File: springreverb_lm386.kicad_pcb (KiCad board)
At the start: 2 copper layers, 69.9 x 55.3 mm, 53 parts, among them J1 IN, J10 VR2_3, J11 VR_2_2, J12 To, J13 FromSW, J16 FromGND, J17 From, J18 VR_4_1, J19 VR4_3, J2 INGND, J20 VR3_1, J3 GND, J4 Vin, J5 LEDGND, J6 VR1_3, J7 VR_1_1, J8 toC6, J9 toC7, U1 TL072, U2 TC1044S, U3 LM386

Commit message: 入力のコンデンサの値を変更
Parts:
- C6: value 0.022u -> 4700p
- C7: value 0.01u -> 470p
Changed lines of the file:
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@@
 			)
 		)
-		(property "Value" "0.01u"
+		(property "Value" "470p"
 			(at 0.05 0.9 90)
 			(unlocked yes)
@@
 			)
 		)
-		(property "Value" "0.022u"
+		(property "Value" "4700p"
 			(at 0.05 0.9 90)
 			(unlocked yes)
@@
 	)
 	(zone
-		(net "Net-(J15-In)")
+		(net "Net-(C3-Pad1)")
 		(layer "B.Cu")
 		(hatch none 0.1)
-		(priority 30015)
+		(priority 30000)
 		(attr
 			(teardrop
@@
 		(polygon
 			(pts
-				(xy 95.5404 89.1376) (xy 93.7404 89.1376) (xy 93.6404 90.1376) (xy 94.6404 91.2886) (xy 95.6404 90.1376)
+				(xy 66.7148 105.373009) (xy 68.5148 105.373009) (xy 68.6148 103.591071) (xy 67.6148 103.272009)
+				(xy 66.6148 103.828978)
 			)
 		)
 	)
 	(zone
-		(net "Net-(U1C-V-)")
+		(net "Net-(C3-Pad1)")
 		(layer "B.Cu")
 		(hatch none 0.1)
-		(priority 30017)
+		(priority 30006)
 		(attr
 			(teardrop
@@
 		(polygon
 			(pts
-				(xy 97.547 78.44473) (xy 95.747 78.44473) (xy 95.747 78.503213) (xy 96.010604 77.866817) (xy 94.947096 79.689252)
-				(xy 95.202722 79.947491) (xy 96.840547 79.723879) (xy 97.283396 79.139609) (xy 97.547 78.503213)
+				(xy 68.5148 103.549091) (xy 66.7148 103.549091) (xy 66.6148 105.192822) (xy 67.6148 105.650091)
+				(xy 68.6148 105.192822)
 			)
 		)
@@
 	)
 	(zone
-		(net "Net-(J1-Pin_1)")
+		(net "Net-(C3-Pad1)")
 		(layer "B.Cu")
 		(hatch none 0.1)
-		(priority 30014)
+		(priority 30010)
 		(attr
 			(teardrop
@@
 		(polygon
 			(pts
-				(xy 117.232 93.609) (xy 115.432 93.609) (xy 115.332 94.609) (xy 116.332 95.76) (xy 117.332 94.609)
+				(xy 66.71787 101.157478) (xy 65.445078 102.43027) (xy 66.53666 103.663273) (xy 67.567105 103.279505)
+				(xy 67.950873 102.24906)
 			)
 		)
 	)
 	(zone
-		(net "Net-(C3-Pad1)")
+		(net "Net-(J6-Pin_1)")
 		(layer "B.Cu")
 		(hatch none 0.1)
-		(priority 30005)
+		(priority 30016)
 		(attr
 			(teardrop
@@
 		(polygon
 			(pts
-				(xy 68.464 101.179791) (xy 66.664 101.179791) (xy 66.564 102.823522) (xy 67.564 103.280791) (xy 68.564 102.823522)
+				(xy 100.446 70.984) (xy 102.246 70.984) (xy 102.346 69.984) (xy 101.346 68.833) (xy 100.346 69.984)
 			)
 		)
 	)
 	(zone
-		(net "Net-(U1C-V+)")
+		(net "Net-(U1C-V-)")
 		(layer "B.Cu")
 		(hatch none 0.1)
-		(priority 30012)
+		(priority 30017)
 		(attr
 			(teardrop
@@
 		(polygon
 			(pts
-				(xy 105.540747 89.145) (xy 105.540747 87.345) (xy 104.396223 87.245) (xy 103.439747 88.245) (xy 103.439747 88.980609)
+				(xy 97.547 78.44473) (xy 95.747 78.44473) (xy 95.747 78.503213) (xy 96.010604 77.866817) (xy 94.947096 79.689252)
+				(xy 95.202722 79.947491) (xy 96.840547 79.723879) (xy 97.283396 79.139609) (xy 97.547 78.503213)
 			)
 		)
 	)
 	(zone
-		(net "Net-(U1C-V-)")
+		(net "GND")
 		(layer "B.Cu")
 		(hatch none 0.1)
-		(priority 30003)
+		(priority 30002)
 		(attr
 			(teardrop
@@
 		(polygon
 			(pts
-				(xy 86.2948 85.888991) (xy 84.4948 85.888991) (xy 84.3948 87.532722) (xy 85.3948 87.989991) (xy 86.3948 87.532722)
+				(xy 92.050391 76.189) (xy 92.050391 77.989) (xy 93.694122 78.089) (xy 94.151391 77.089) (xy 93.694122 76.089)
 			)
 		)
 	)
 	(zone
-		(net "Net-(C12-Pad2)")
+		(net "GND")
 		(layer "B.Cu")
 		(hatch none 0.1)
-		(priority 30008)
+		(priority 30013)
 		(attr
 			(teardrop
@@
 		(polygon
 			(pts
-				(xy 86.24093 97.724522) (xy 87.513722 96.45173) (xy 86.422139 95.218726) (xy 85.391695 95.602495)
-				(xy 85.007926 96.632939)
+				(xy 90.0062 90.7436) (xy 91.8062 90.7436) (xy 91.9062 89.7436) (xy 90.9062 88.4926) (xy 89.9062 89.7436)
 			)
 		)
@@
 		(layer "B.Cu")
 		(hatch none 0.1)
-		(priority 30010)
+		(priority 30005)
 		(attr
 			(teardrop
@@
 		(polygon
 			(pts
-				(xy 66.71787 101.157478) (xy 65.445078 102.43027) (xy 66.53666 103.663273) (xy 67.567105 103.279505)
-				(xy 67.950873 102.24906)
+				(xy 68.464 101.179791) (xy 66.664 101.179791) (xy 66.564 102.823522) (xy 67.564 103.280791) (xy 68.564 102.823522)
 			)
 		)
@@
 	)
 	(zone
-		(net "GND")
+		(net "Net-(J15-In)")
 		(layer "B.Cu")
 		(hatch none 0.1)
-		(priority 30013)
+		(priority 30015)
 		(attr
 			(teardrop
@@
 		(polygon
 			(pts
-				(xy 90.0062 90.7436) (xy 91.8062 90.7436) (xy 91.9062 89.7436) (xy 90.9062 88.4926) (xy 89.9062 89.7436)
+				(xy 95.5404 89.1376) (xy 93.7404 89.1376) (xy 93.6404 90.1376) (xy 94.6404 91.2886) (xy 95.6404 90.1376)
 			)
 		)
@@
 		(layer "B.Cu")
 		(hatch none 0.1)
-		(priority 30006)
+		(priority 30011)
 		(attr
 			(teardrop
@@
 		(polygon
 			(pts
-				(xy 68.5148 103.549091) (xy 66.7148 103.549091) (xy 66.6148 105.192822) (xy 67.6148 105.650091)
-				(xy 68.6148 105.192822)
+				(xy 92.541425 94.433999) (xy 92.541425 96.233999) (xy 93.082401 96.233999) (xy 93.718797 95.970395)
+				(xy 94.569274 95.261339) (xy 94.185505 94.230895) (xy 93.15506 93.847125) (xy 92.446005 94.697603)
+				(xy 93.082401 94.433999)
 			)
 		)
 	)
 	(zone
-		(net "Net-(C3-Pad1)")
+		(net "GND")
 		(layer "B.Cu")
 		(hatch none 0.1)
-		(priority 30000)
+		(priority 30001)
 		(attr
 			(teardrop
@@
 		(polygon
 			(pts
-				(xy 66.7148 105.373009) (xy 68.5148 105.373009) (xy 68.6148 103.591071) (xy 67.6148 103.272009)
-				(xy 66.6148 103.828978)
+				(xy 83.8256 115.073591) (xy 82.0256 115.073591) (xy 81.9256 116.717322) (xy 82.9256 117.174591)
+				(xy 83.9256 116.717322)
 			)
 		)
 	)
 	(zone
-		(net "Net-(J6-Pin_1)")
+		(net "Net-(U1C-V-)")
 		(layer "B.Cu")
 		(hatch none 0.1)
-		(priority 30016)
+		(priority 30003)
 		(attr
 			(teardrop
@@
 		(polygon
 			(pts
-				(xy 100.446 70.984) (xy 102.246 70.984) (xy 102.346 69.984) (xy 101.346 68.833) (xy 100.346 69.984)
+				(xy 86.2948 85.888991) (xy 84.4948 85.888991) (xy 84.3948 87.532722) (xy 85.3948 87.989991) (xy 86.3948 87.532722)
 			)
 		)
 	)
 	(zone
-		(net "Net-(C3-Pad1)")
+		(net "Net-(C12-Pad2)")
 		(layer "B.Cu")
 		(hatch none 0.1)
-		(priority 30011)
+		(priority 30008)
 		(attr
 			(teardrop
@@
 		(polygon
 			(pts
-				(xy 92.541425 94.433999) (xy 92.541425 96.233999) (xy 93.082401 96.233999) (xy 93.718797 95.970395)
-				(xy 94.569274 95.261339) (xy 94.185505 94.230895) (xy 93.15506 93.847125) (xy 92.446005 94.697603)
-				(xy 93.082401 94.433999)
+				(xy 86.24093 97.724522) (xy 87.513722 96.45173) (xy 86.422139 95.218726) (xy 85.391695 95.602495)
+				(xy 85.007926 96.632939)
 			)
 		)
 	)
 	(zone
-		(net "GND")
+		(net "Net-(U1C-V+)")
 		(layer "B.Cu")
 		(hatch none 0.1)
-		(priority 30002)
+		(priority 30007)
 		(attr
 			(teardrop
@@
 		(polygon
 			(pts
-				(xy 92.050391 76.189) (xy 92.050391 77.989) (xy 93.694122 78.089) (xy 94.151391 77.089) (xy 93.694122 76.089)
+				(xy 104.35113 90.002922) (xy 105.623922 88.73013) (xy 104.532339 87.497126) (xy 103.501895 87.880895)
+				(xy 103.118126 88.911339)
 			)
 		)
 	)
 	(zone
-		(net "GND")
+		(net "Net-(U1C-V+)")
 		(layer "B.Cu")
 		(hatch none 0.1)
-		(priority 30001)
+		(priority 30012)
 		(attr
 			(teardrop
@@
 		(polygon
 			(pts
-				(xy 83.8256 115.073591) (xy 82.0256 115.073591) (xy 81.9256 116.717322) (xy 82.9256 117.174591)
-				(xy 83.9256 116.717322)
+				(xy 105.540747 89.145) (xy 105.540747 87.345) (xy 104.396223 87.245) (xy 103.439747 88.245) (xy 103.439747 88.980609)
 			)
 		)
 	)
 	(zone
-		(net "Net-(U1C-V+)")
+		(net "Net-(J1-Pin_1)")
 		(layer "B.Cu")
 		(hatch none 0.1)
-		(priority 30007)
+		(priority 30014)
 		(attr
 			(teardrop
@@
 		(polygon
 			(pts
-				(xy 104.35113 90.002922) (xy 105.623922 88.73013) (xy 104.532339 87.497126) (xy 103.501895 87.880895)
-				(xy 103.118126 88.911339)
+				(xy 117.232 93.609) (xy 115.432 93.609) (xy 115.332 94.609) (xy 116.332 95.76) (xy 117.332 94.609)
 			)
 		)

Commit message: 実際に配線しての修正を反映
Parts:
- removed J19: VR4_3, MyLibrary:PinHeader_1x01_P2.54mm_Vertical
- removed the J2 at (112.6, 95.8)
- removed the J3 at (90.8, 84.6)
- removed the J5 at (90.9, 92.1)
- J15: renamed from J20; value VR3_1 -> VR4_1
- J16: renamed from J18; value VR_4_1 -> VR_3_1
- moved J15 13.7 mm to (97.2, 70.5)
- moved J3 5.97 mm to (107.3, 68.8)
- moved J1 1.08 mm to (115.6, 96.5)
- renumbered C2 to C1, C11 to C10, C12 to C11, C13 to C12, C14 to C13, C15 to C14, C16 to C15, C17 to C16, C18 to C17, C19 to C18, C20 to C19, C3 to C2, C4 to C3, C5 to C4, C6 to C5, C7 to C6, C8 to C7, C9 to C8, C10 to C9, J13 to J10, J16 to J13, J17 to J14, J4 to J2, J6 to J3, J7 to J4, J8 to J5, J9 to J6, J10 to J7, J11 to J8, J12 to J9, R8 to R10, R9 to R11, R4 to R6, R5 to R7, R6 to R8, R7 to R9
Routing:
- net GND: track 208.3 -> 195.1 mm
- net Net-(J15-Pin_1): track 13.4 -> 15.5 mm
- net Net-(J3-Pin_1): track 5.51 -> 6.19 mm
- net Net-(J1-Pin_1): track 4.96 -> 5.51 mm

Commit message: GNDの位置を修正
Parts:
- removed the J4 at (64.5, 77.6)
- added J3: GND, MyLibrary:PinHeader_1x01_P2.54mm_Vertical, F.Cu at (66.3, 112.3)
- renumbered J9 to J10, J10 to J11, J13 to J14, J14 to J15, J15 to J16, J16 to J17, J3 to J4, J5 to J6, J6 to J7, J7 to J8, J8 to J9
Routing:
- net GND: track 195.1 -> 197.5 mm

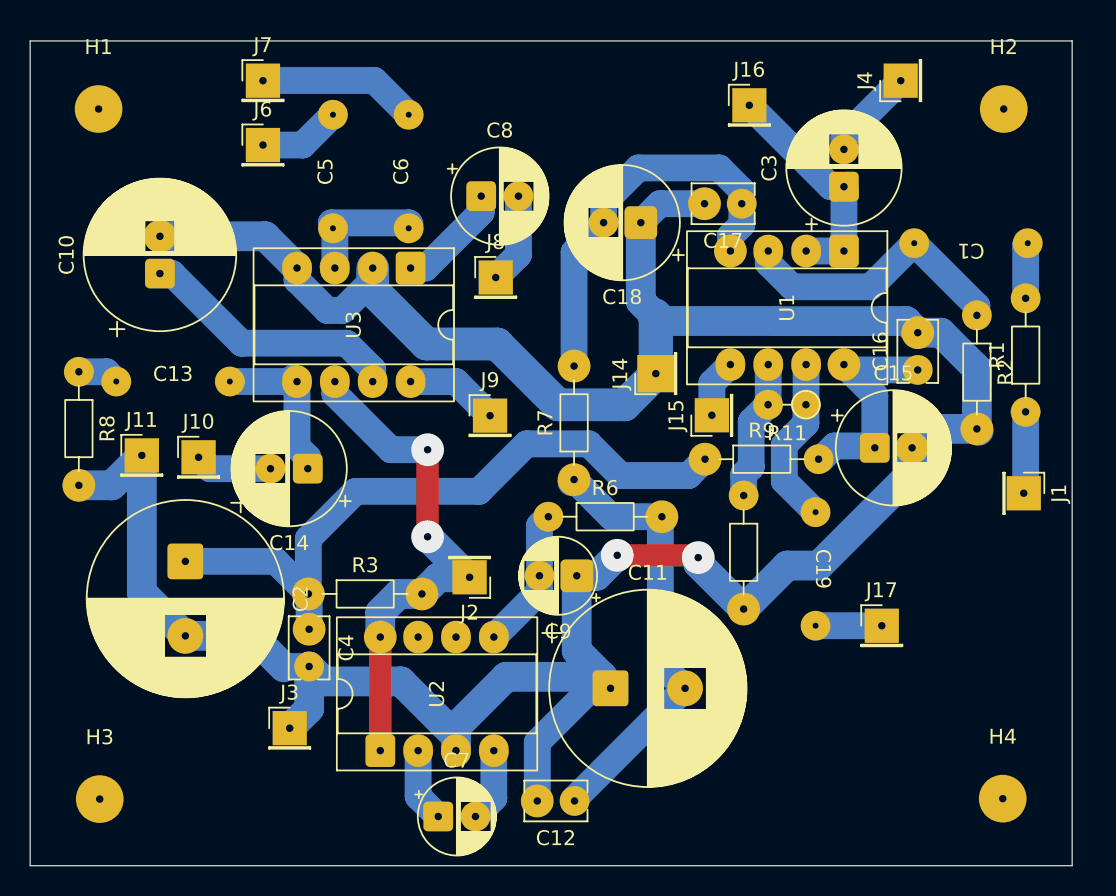
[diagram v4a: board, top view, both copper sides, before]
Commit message: トーン回路の修正
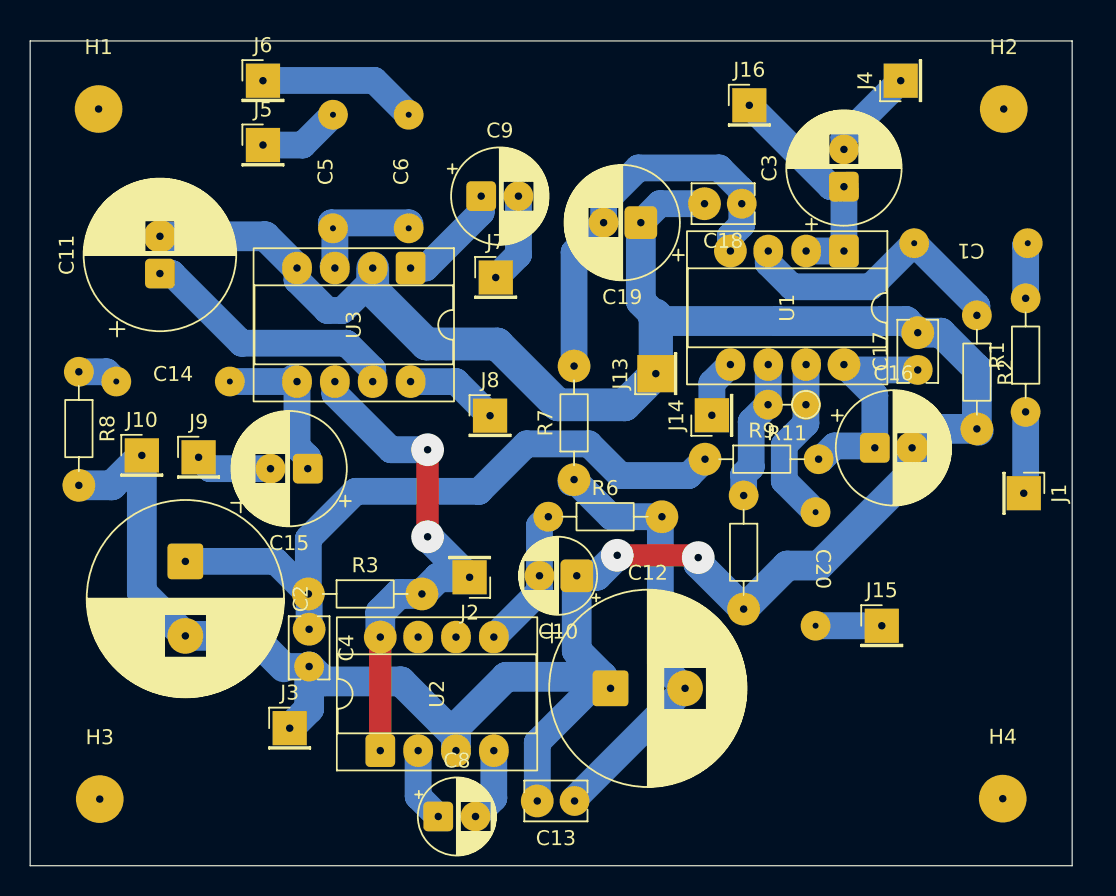
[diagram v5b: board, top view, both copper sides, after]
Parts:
- renumbered C9 to C10, C10 to C11, C11 to C12, C12 to C13, C13 to C14, C14 to C15, C15 to C16, C16 to C17, C17 to C18, C18 to C19, C19 to C20, C7 to C8, C8 to C9, J11 to J10, J14 to J13, J15 to J14, J17 to J15, J6 to J5, J7 to J6, J8 to J7, J9 to J8, J10 to J9
